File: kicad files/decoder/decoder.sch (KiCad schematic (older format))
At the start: 7 parts, among them J2 Power Connector, SW1 up, SW2 down, SW3 sel

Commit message: added line button
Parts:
- added SW4: line, Button_Switch_THT:SW_PUSH_6mm, symbol Switch:SW_Push
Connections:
- net GND: now also SW4.1
- net at A1.9 (D6): now also SW4.2
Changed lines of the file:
@@
 Wire Wire Line
 	1550 1650 1550 1550
+$Comp
+L Switch:SW_Push SW4
+U 1 1 6075582A
+P 3700 1250
+F 0 "SW4" H 3700 1535 50  0000 C CNN
+F 1 "line" H 3700 1444 50  0000 C CNN
+F 2 "Button_Switch_THT:SW_PUSH_6mm" H 3700 1450 50  0001 C CNN
+F 3 "~" H 3700 1450 50  0001 C CNN
+	1    3700 1250
+	1    0    0    -1
+$EndComp
+Wire Wire Line
+	3500 1250 3400 1250
+Wire Wire Line
+	3400 1250 3400 1650
+Connection ~ 3400 1650
+Wire Wire Line
+	4600 1850 4100 1850
+Wire Wire Line
+	4100 1850 4100 1250
+Wire Wire Line
+	3900 1250 4100 1250
 $EndSCHEMATC

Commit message: final changes to PCB, started to clean up code on first gen PCB
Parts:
- added J1, J3: Conn_01x01_Male, Connector_PinHeader_2.54mm:PinHeader_1x01_P2.54mm_Vertical, symbol Connector:Conn_01x01_Male
- added R1: 220, Resistor_THT:R_Axial_DIN0309_L9.0mm_D3.2mm_P12.70mm_Horizontal, symbol Device:R
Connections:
- net +5V: now also J1.1 (Pin_1)
- net GND: now also R1.2; no longer DS1.16 (LED(-))
- new net: DS1.16 (LED(-)), R1.1
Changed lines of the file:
@@
 L power:GND #PWR0104
 U 1 1 607879E5
-P 3000 1750
-F 0 "#PWR0104" H 3000 1500 50  0001 C CNN
-F 1 "GND" H 3005 1577 50  0000 C CNN
-F 2 "" H 3000 1750 50  0001 C CNN
-F 3 "" H 3000 1750 50  0001 C CNN
-	1    3000 1750
+P 3000 2050
+F 0 "#PWR0104" H 3000 1800 50  0001 C CNN
+F 1 "GND" H 3005 1877 50  0000 C CNN
+F 2 "" H 3000 2050 50  0001 C CNN
+F 3 "" H 3000 2050 50  0001 C CNN
+	1    3000 2050
 	1    0    0    -1
 $EndComp
@@
 L power:+5V #PWR0110
 U 1 1 6079401D
-P 1350 1350
-F 0 "#PWR0110" H 1350 1200 50  0001 C CNN
-F 1 "+5V" H 1365 1523 50  0000 C CNN
-F 2 "" H 1350 1350 50  0001 C CNN
-F 3 "" H 1350 1350 50  0001 C CNN
-	1    1350 1350
+P 1250 1350
+F 0 "#PWR0110" H 1250 1200 50  0001 C CNN
+F 1 "+5V" H 1265 1523 50  0000 C CNN
+F 2 "" H 1250 1350 50  0001 C CNN
+F 3 "" H 1250 1350 50  0001 C CNN
+	1    1250 1350
 	1    0    0    -1
 $EndComp
-Wire Wire Line
-	1350 1350 1350 1400
-Wire Wire Line
-	1350 1400 1400 1400
 Wire Wire Line
 	1450 1650 1550 1650
@@
 Wire Wire Line
 	3900 1250 4100 1250
+$Comp
+L Device:R R1
+U 1 1 6076EE42
+P 3000 1900
+F 0 "R1" H 3070 1946 50  0000 L CNN
+F 1 "220" H 3070 1855 50  0000 L CNN
+F 2 "Resistor_THT:R_Axial_DIN0309_L9.0mm_D3.2mm_P12.70mm_Horizontal" V 2930 1900 50  0001 C CNN
+F 3 "~" H 3000 1900 50  0001 C CNN
+	1    3000 1900
+	1    0    0    -1
+$EndComp
+$Comp
+L Connector:Conn_01x01_Male J1
+U 1 1 608BA39A
+P 1400 900
+F 0 "J1" V 1462 944 50  0000 L CNN
+F 1 "Conn_01x01_Male" V 1553 944 50  0000 L CNN
+F 2 "Connector_PinHeader_2.54mm:PinHeader_1x01_P2.54mm_Vertical" H 1400 900 50  0001 C CNN
+F 3 "~" H 1400 900 50  0001 C CNN
+	1    1400 900
+	0    1    1    0
+$EndComp
+$Comp
+L Connector:Conn_01x01_Male J3
+U 1 1 608BCD02
+P 1700 900
+F 0 "J3" V 1762 944 50  0000 L CNN
+F 1 "Conn_01x01_Male" V 1853 944 50  0000 L CNN
+F 2 "Connector_PinHeader_2.54mm:PinHeader_1x01_P2.54mm_Vertical" H 1700 900 50  0001 C CNN
+F 3 "~" H 1700 900 50  0001 C CNN
+	1    1700 900
+	0    1    1    0
+$EndComp
+Wire Wire Line
+	1250 1400 1250 1350
+Wire Wire Line
+	1250 1400 1400 1400
+Wire Wire Line
+	1400 1100 1400 1400
+Connection ~ 1400 1400
+Wire Wire Line
+	1700 1150 1700 1400
+Connection ~ 1700 1400
 $EndSCHEMATC

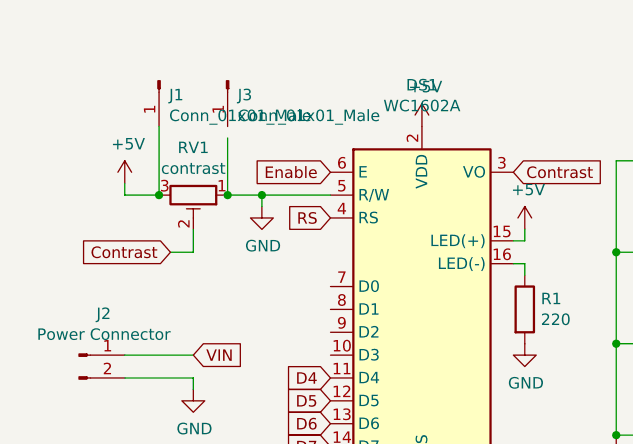
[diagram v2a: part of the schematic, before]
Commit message: fixed an issue on the first rev of the PCB
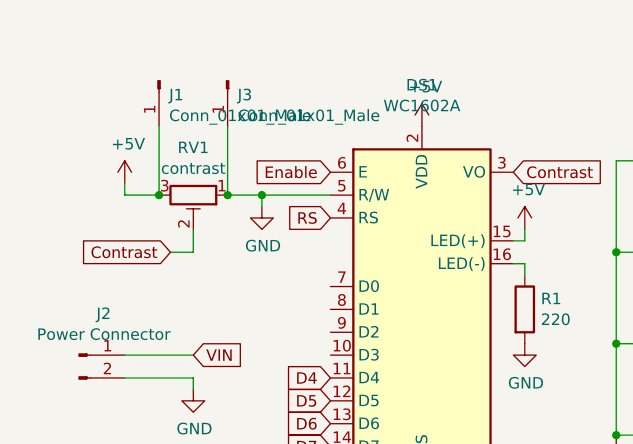
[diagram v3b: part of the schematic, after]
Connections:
- net GND: now also J3.1 (Pin_1)
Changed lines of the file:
@@
 	1400 1100 1400 1400
 Connection ~ 1400 1400
+Connection ~ 1700 1400
 Wire Wire Line
-	1700 1150 1700 1400
-Connection ~ 1700 1400
+	1700 1100 1700 1400
 $EndSCHEMATC
